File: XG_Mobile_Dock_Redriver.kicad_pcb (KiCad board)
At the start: 4 copper layers, 220 x 65 mm, 151 parts, among them J1 5-1775443-8, J10 SWD, J11 UART, J12 I2C1, J13 39301240, J14 SWD, J15 SWD, J17 8730, J2 20455-040E-76, J20 SWD, J21 SWD, J22 SWD, J23 SWD, J24 SWD, J25 SWD, J26 SWD, J27 SWD, J28 SWD, J29 SWD, J3 20455-040E-76, J30 SWD, J31 SWD, J32 SWD, J33 SWD, J4 3-2362375-4, J5 USB_C_Receptacle, J6 455860005, Q16 AO3401A, Q17 2N7002W, SW1 SW_Push, U1 DS320PR810NJXR, U12 STM32F030C8Tx, U2 DS320PR810NJXR

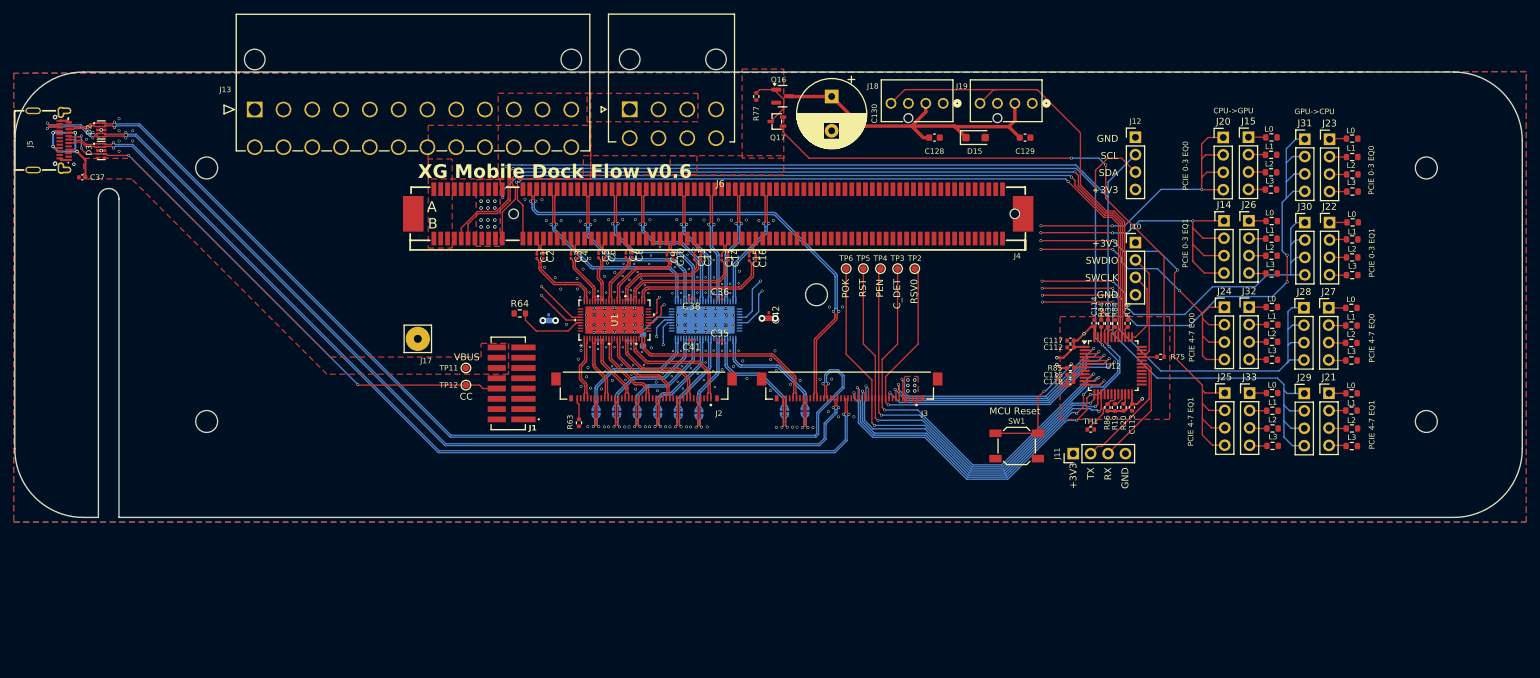
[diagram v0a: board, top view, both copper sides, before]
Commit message: added more vias
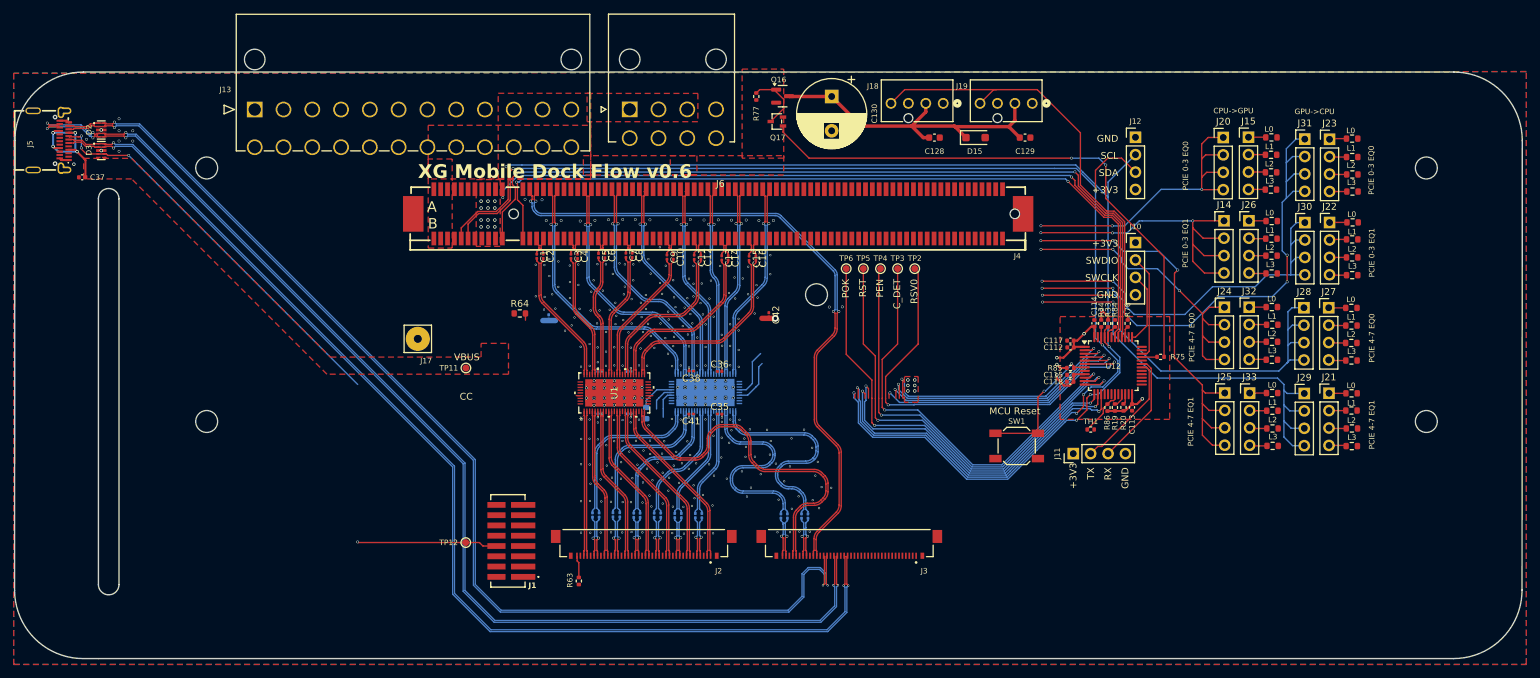
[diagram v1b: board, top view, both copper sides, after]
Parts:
- moved R63 23.1 mm to (99.1, 113.7)
- moved J1 23.0 mm to (88.8, 107.9)
- moved J2 23.0 mm to (108.6, 108.1)
- moved J3 23.0 mm to (138.6, 108.1)
- moved TP12 23.0 mm to (82.6, 108.1)
- moved C31 15.3 mm to (131.6, 104.2)
- moved C32 15.3 mm to (132.5, 104.2)
- moved C30 15.3 mm to (129.5, 104.2)
- moved C29 15.3 mm to (128.6, 104.2)
- moved C17 15.1 mm to (101.1, 104.1)
- moved C18 15.1 mm to (102.1, 104.1)
- moved C19 15.1 mm to (104.1, 104.0)
- moved C20 15.1 mm to (105.1, 104.0)
- moved C21 15.1 mm to (107.1, 104.1)
- moved C22 15.1 mm to (108.0, 104.1)
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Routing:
- net +3V3: track 274.8 -> 245.8 mm, vias 36 -> 33
- net /CLKN: track 70.7 -> 96.6 mm
- net /CLKP: track 70.7 -> 96.5 mm
- net /C_RXN: track 142.8 -> 167.2 mm
- net /C_RXP: track 142.4 -> 166.8 mm
- net /HSOL7P: track 28.3 -> 52.7 mm
- net /HSOL7N: track 28.3 -> 52.7 mm
- net /C_DN: track 139.9 -> 164.1 mm
- net /C_DP: track 139.5 -> 163.6 mm
- net /C_TXP: track 145.2 -> 162.6 mm
- net /C_TXN: track 146.5 -> 162.1 mm
- net /HSIT6P: track 16.1 -> 31.3 mm
- net /HSIT6N: track 16.1 -> 31.3 mm
- net /HSIT7P: track 17.8 -> 32.3 mm
- net /HSIT7N: track 17.8 -> 32.3 mm
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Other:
- board size 220 x 65 mm -> 220 x 85.6 mm

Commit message: finished board setup
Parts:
- moved C42 40.2 mm to (88.1, 85.8)
- moved C43 36.5 mm to (129.6, 85.8)
- moved TP11 23.1 mm to (79.8, 105.5)
- moved J17 22.4 mm to (75.6, 100.8)
- moved R64 12.6 mm to (94.2, 86.7)
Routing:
- net +3V3: track 245.8 -> 148.0 mm, vias 33 -> 36
- net /RSV0: track 62.2 -> 85.6 mm, vias 2 -> 3
- net /CC: track 79.0 -> 102.0 mm
- net /LOCK_DET: track 39.8 -> 60.2 mm
- net /LED_RED#: track 38.2 -> 58.2 mm
- net /LED_WHITE#: track 37.6 -> 56.8 mm
- net /LOCK_SW: track 37.1 -> 55.5 mm
- net /CON_DET: track 62.6 -> 80.7 mm
- net /PWREN#: track 64.1 -> 81.9 mm
- net /RST#: track 67.3 -> 84.7 mm
- net /CPU_TO_GPU_EQ0_0: track 122.4 -> 139.5 mm, vias 3 -> 4
- net /PWROK: track 64.5 -> 81.5 mm
- net /CPU_TO_GPU_EQ1_1: track 125.1 -> 140.3 mm, vias 3 -> 4
- net /CPU_TO_GPU_EQ1_0: track 125.7 -> 140.9 mm, vias 3 -> 4
- net /CPU_TO_GPU_EQ0_1: track 108.9 -> 123.3 mm, vias 3 -> 4
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
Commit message: more changes of pcb
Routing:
- net GND: vias 339 -> 397
